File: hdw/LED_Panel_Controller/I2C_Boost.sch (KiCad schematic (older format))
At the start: 7 parts

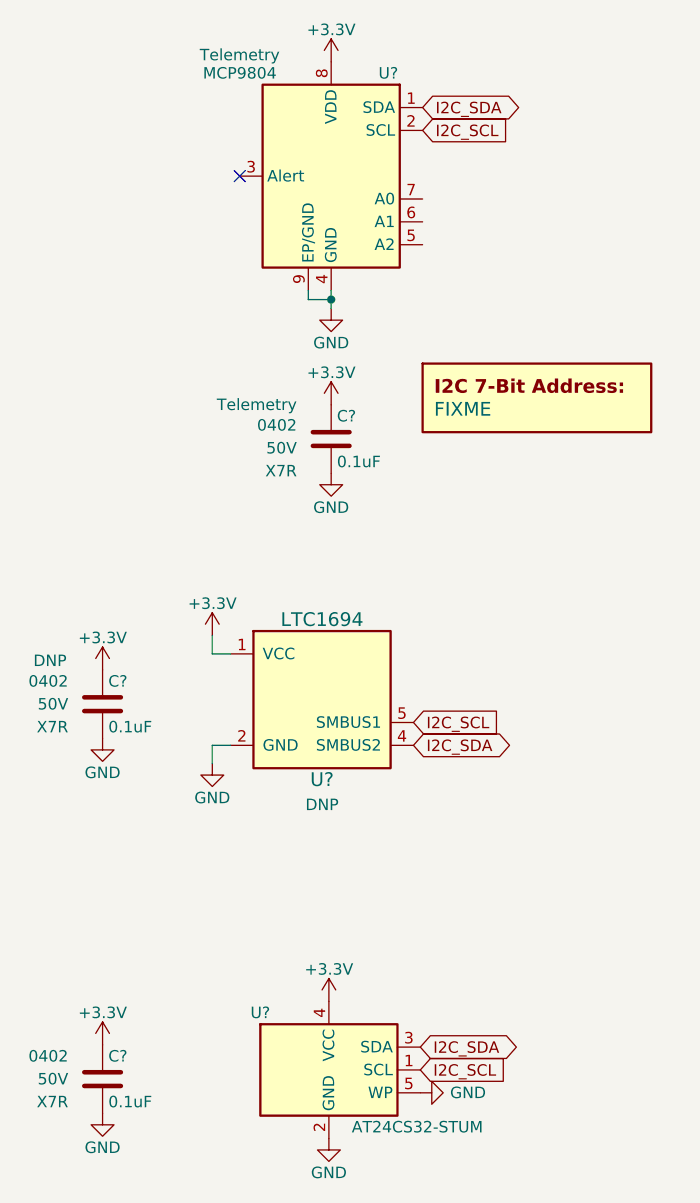
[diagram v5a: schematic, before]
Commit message: assigned I2C addresses
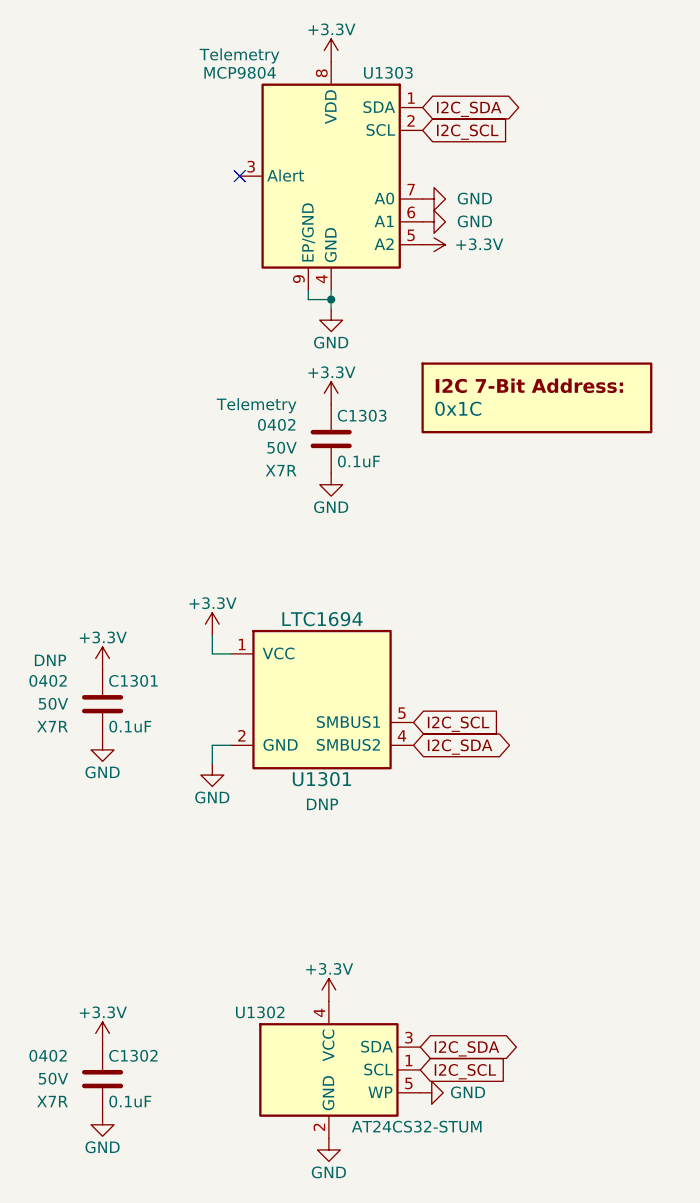
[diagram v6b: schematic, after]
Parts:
- DOC1301: renamed from DOC?; value FIXME -> 0x1C
- gave numbers to parts that had none: 6
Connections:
- net +3V3: now also U1303.5 (A2)
- net GND: now also U1303.6 (A1), U1303.7 (A0)
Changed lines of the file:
@@
 $EndDescr
 $Comp
-L Custom_Library:LTC1694 U?
+L Custom_Library:LTC1694 U1301
 U 1 1 5F6A42D0
 P 5300 3760
-F 0 "U?" H 5300 3410 60  0000 C CNN
+F 0 "U1301" H 5300 3410 60  0000 C CNN
 F 1 "LTC1694" H 5300 4110 60  0000 C CNN
 F 2 "Package_TO_SOT_SMD:SOT-23-5" H 5200 4060 60  0001 C CNN
@@
 $EndComp
 $Comp
-L power:+3.3V #PWR?
+L power:+3.3V #PWR01305
 U 1 1 5F6A5589
 P 4820 3480
-F 0 "#PWR?" H 4820 3330 50  0001 C CNN
+F 0 "#PWR01305" H 4820 3330 50  0001 C CNN
 F 1 "+3.3V" H 4820 3620 50  0000 C CNN
 F 2 "" H 4820 3480 50  0001 C CNN
@@
 	4820 3560 4900 3560
 $Comp
-L power:GND #PWR?
+L power:GND #PWR01306
 U 1 1 5F6A5AAB
 P 4820 4040
-F 0 "#PWR?" H 4820 3790 50  0001 C CNN
+F 0 "#PWR01306" H 4820 3790 50  0001 C CNN
 F 1 "GND" H 4820 3890 50  0000 C CNN
 F 2 "" H 4820 4040 50  0001 C CNN
@@
 	4820 3960 4900 3960
 $Comp
-L power:GND #PWR?
+L power:GND #PWR01302
 U 1 1 5F6A9D7C
 P 4340 3930
-F 0 "#PWR?" H 4340 3680 50  0001 C CNN
+F 0 "#PWR01302" H 4340 3680 50  0001 C CNN
 F 1 "GND" H 4340 3780 50  0000 C CNN
 F 2 "" H 4340 3930 50  0001 C CNN
@@
 AR Path="/5EAE3021/5F6A9DE1" Ref="C?"  Part="1"
 AR Path="/5F582A92/5F6A9DE1" Ref="C?"  Part="1"
-AR Path="/5F582A7C/5F6A9DE1" Ref="C?"  Part="1"
-F 0 "C?" H 4365 3880 50  0000 L CNN
+AR Path="/5F582A7C/5F6A9DE1" Ref="C1301"  Part="1"
+F 0 "C1301" H 4365 3880 50  0000 L CNN
 F 1 "0.1uF" H 4365 3680 50  0000 L CNN
 F 2 "Capacitors_SMD:C_0402" H 4378 3630 50  0001 C CNN
@@
 $EndComp
 $Comp
-L power:+3.3V #PWR?
+L power:+3.3V #PWR01301
 U 1 1 5F6AB1EB
 P 4340 3630
-F 0 "#PWR?" H 4340 3480 50  0001 C CNN
+F 0 "#PWR01301" H 4340 3480 50  0001 C CNN
 F 1 "+3.3V" H 4340 3770 50  0000 C CNN
 F 2 "" H 4340 3630 50  0001 C CNN
@@
 P 5330 5380
 AR Path="/5F5829EF/601A8ABF" Ref="U?"  Part="1"
-AR Path="/5F582A7C/601A8ABF" Ref="U?"  Part="1"
-F 0 "U?" H 5030 5630 50  0000 C CNN
+AR Path="/5F582A7C/601A8ABF" Ref="U1302"  Part="1"
+F 0 "U1302" H 5030 5630 50  0000 C CNN
 F 1 "AT24CS32-STUM" H 5430 5130 50  0000 L CNN
 F 2 "Package_TO_SOT_SMD:SOT-23-5" H 5330 5380 50  0001 C CNN
@@
 P 5330 5680
 AR Path="/5F5829EF/601A8AC5" Ref="#PWR?"  Part="1"
-AR Path="/5F582A7C/601A8AC5" Ref="#PWR?"  Part="1"
-F 0 "#PWR?" H 5330 5430 50  0001 C CNN
+AR Path="/5F582A7C/601A8AC5" Ref="#PWR01308"  Part="1"
+F 0 "#PWR01308" H 5330 5430 50  0001 C CNN
 F 1 "GND" H 5330 5530 50  0000 C CNN
 F 2 "" H 5330 5680 50  0001 C CNN
@@
 P 5330 5080
 AR Path="/5F5829EF/601A8ACB" Ref="#PWR?"  Part="1"
-AR Path="/5F582A7C/601A8ACB" Ref="#PWR?"  Part="1"
-F 0 "#PWR?" H 5330 4930 50  0001 C CNN
+AR Path="/5F582A7C/601A8ACB" Ref="#PWR01307"  Part="1"
+F 0 "#PWR01307" H 5330 4930 50  0001 C CNN
 F 1 "+3.3V" H 5330 5220 50  0000 C CNN
 F 2 "" H 5330 5080 50  0001 C CNN
@@
 $EndComp
 $Comp
-L power:GND #PWR?
+L power:GND #PWR01304
 U 1 1 601A97E7
 P 4340 5570
-F 0 "#PWR?" H 4340 5320 50  0001 C CNN
+F 0 "#PWR01304" H 4340 5320 50  0001 C CNN
 F 1 "GND" H 4340 5420 50  0000 C CNN
 F 2 "" H 4340 5570 50  0001 C CNN
@@
 AR Path="/5EAE3021/601A97F2" Ref="C?"  Part="1"
 AR Path="/5F582A92/601A97F2" Ref="C?"  Part="1"
-AR Path="/5F582A7C/601A97F2" Ref="C?"  Part="1"
-F 0 "C?" H 4365 5520 50  0000 L CNN
+AR Path="/5F582A7C/601A97F2" Ref="C1302"  Part="1"
+F 0 "C1302" H 4365 5520 50  0000 L CNN
 F 1 "0.1uF" H 4365 5320 50  0000 L CNN
 F 2 "Capacitors_SMD:C_0402" H 4378 5270 50  0001 C CNN
@@
 $EndComp
 $Comp
-L power:+3.3V #PWR?
+L power:+3.3V #PWR01303
 U 1 1 601A97F8
 P 4340 5270
-F 0 "#PWR?" H 4340 5120 50  0001 C CNN
+F 0 "#PWR01303" H 4340 5120 50  0001 C CNN
 F 1 "+3.3V" H 4340 5410 50  0000 C CNN
 F 2 "" H 4340 5270 50  0001 C CNN
@@
 P 5730 5480
 AR Path="/5F5829EF/601AB410" Ref="#PWR?"  Part="1"
-AR Path="/5F582A7C/601AB410" Ref="#PWR?"  Part="1"
-F 0 "#PWR?" H 5730 5230 50  0001 C CNN
+AR Path="/5F582A7C/601AB410" Ref="#PWR01313"  Part="1"
+F 0 "#PWR01313" H 5730 5230 50  0001 C CNN
 F 1 "GND" V 5730 5350 50  0000 R CNN
 F 2 "" H 5730 5480 50  0001 C CNN
@@
 AR Path="/5F581B77/6061CC13" Ref="#PWR?"  Part="1"
 AR Path="/5F581BB7/6061CC13" Ref="#PWR?"  Part="1"
-AR Path="/5F582A7C/6061CC13" Ref="#PWR?"  Part="1"
-F 0 "#PWR?" H 5340 1800 50  0001 C CNN
+AR Path="/5F582A7C/6061CC13" Ref="#PWR01310"  Part="1"
+F 0 "#PWR01310" H 5340 1800 50  0001 C CNN
 F 1 "GND" H 5340 1900 50  0000 C CNN
 F 2 "" H 5340 2050 50  0001 C CNN
@@
 AR Path="/5F581B77/6061CC1E" Ref="#PWR?"  Part="1"
 AR Path="/5F581BB7/6061CC1E" Ref="#PWR?"  Part="1"
-AR Path="/5F582A7C/6061CC1E" Ref="#PWR?"  Part="1"
-F 0 "#PWR?" H 5340 820 50  0001 C CNN
+AR Path="/5F582A7C/6061CC1E" Ref="#PWR01309"  Part="1"
+F 0 "#PWR01309" H 5340 820 50  0001 C CNN
 F 1 "+3.3V" H 5340 1110 50  0000 C CNN
 F 2 "" H 5340 970 50  0001 C CNN
@@
 AR Path="/5F581B77/6061CC26" Ref="U?"  Part="1"
 AR Path="/5F581BB7/6061CC26" Ref="U?"  Part="1"
-AR Path="/5F582A7C/6061CC26" Ref="U?"  Part="1"
-F 0 "U?" H 5090 1920 50  0000 C CNN
+AR Path="/5F582A7C/6061CC26" Ref="U1303"  Part="1"
+F 0 "U1303" H 5090 1920 50  0000 C CNN
 F 1 "MCP9804" H 5740 1920 50  0000 C CNN
 F 2 "Package_DFN_QFN:DFN-8-1EP_3x2mm_P0.5mm_EP1.3x1.5mm" H 4240 970 50  0001 C CNN
@@
 AR Path="/5F581B77/6061CC2F" Ref="#PWR?"  Part="1"
 AR Path="/5F581BB7/6061CC2F" Ref="#PWR?"  Part="1"
-AR Path="/5F582A7C/6061CC2F" Ref="#PWR?"  Part="1"
-F 0 "#PWR?" H 5340 2320 50  0001 C CNN
+AR Path="/5F582A7C/6061CC2F" Ref="#PWR01311"  Part="1"
+F 0 "#PWR01311" H 5340 2320 50  0001 C CNN
 F 1 "+3.3V" H 5340 2610 50  0000 C CNN
 F 2 "" H 5340 2470 50  0001 C CNN
@@
 AR Path="/5F581B77/6061CC35" Ref="#PWR?"  Part="1"
 AR Path="/5F581BB7/6061CC35" Ref="#PWR?"  Part="1"
-AR Path="/5F582A7C/6061CC35" Ref="#PWR?"  Part="1"
-F 0 "#PWR?" H 5340 2520 50  0001 C CNN
+AR Path="/5F582A7C/6061CC35" Ref="#PWR01312"  Part="1"
+F 0 "#PWR01312" H 5340 2520 50  0001 C CNN
 F 1 "GND" H 5340 2620 50  0000 C CNN
 F 2 "" H 5340 2770 50  0001 C CNN
@@
 AR Path="/5F581B77/6061CC3B" Ref="DOC?"  Part="1"
 AR Path="/5F581BB7/6061CC3B" Ref="DOC?"  Part="1"
-AR Path="/5F582A7C/6061CC3B" Ref="DOC?"  Part="1"
-F 0 "DOC?" H 6240 2740 60  0001 C CNN
-F 1 "FIXME" H 5790 2490 60  0000 L CNN
+AR Path="/5F582A7C/6061CC3B" Ref="DOC1301"  Part="1"
+F 0 "DOC1301" H 6240 2740 60  0001 C CNN
+F 1 "0x1C" H 5790 2490 60  0000 L CNN
 F 2 "" H 6240 2840 60  0001 C CNN
 F 3 "" H 6240 2840 60  0001 C CNN
@@
 AR Path="/5F581B77/6061CC45" Ref="C?"  Part="1"
 AR Path="/5F581BB7/6061CC45" Ref="C?"  Part="1"
-AR Path="/5F582A7C/6061CC45" Ref="C?"  Part="1"
-F 0 "C?" H 5365 2720 50  0000 L CNN
+AR Path="/5F582A7C/6061CC45" Ref="C1303"  Part="1"
+F 0 "C1303" H 5365 2720 50  0000 L CNN
 F 1 "0.1uF" H 5365 2520 50  0000 L CNN
 F 2 "Capacitors_SMD:C_0402" H 5378 2470 50  0001 C CNN
@@
 	1    0    0    -1
 $EndComp
+$Comp
+L power:GND #PWR?
+U 1 1 6076C67B
+P 5740 1570
+AR Path="/5B3E071A/6076C67B" Ref="#PWR?"  Part="1"
+AR Path="/5E0652BA/6076C67B" Ref="#PWR?"  Part="1"
+AR Path="/5E0A0E29/6076C67B" Ref="#PWR?"  Part="1"
+AR Path="/5E052856/6076C67B" Ref="#PWR?"  Part="1"
+AR Path="/5EAE2D84/6076C67B" Ref="#PWR?"  Part="1"
+AR Path="/5F581B58/6076C67B" Ref="#PWR?"  Part="1"
+AR Path="/5F581B77/6076C67B" Ref="#PWR?"  Part="1"
+AR Path="/5F5829EF/6076C67B" Ref="#PWR?"  Part="1"
+AR Path="/5F582A7C/6076C67B" Ref="#PWR01314"  Part="1"
+F 0 "#PWR01314" H 5740 1320 50  0001 C CNN
+F 1 "GND" V 5740 1420 50  0000 R CNN
+F 2 "" H 5740 1570 50  0001 C CNN
+F 3 "" H 5740 1570 50  0001 C CNN
+	1    5740 1570
+	0    -1   1    0
+$EndComp
+$Comp
+L power:+3.3V #PWR?
+U 1 1 6076C681
+P 5740 1770
+AR Path="/5E0652BA/6076C681" Ref="#PWR?"  Part="1"
+AR Path="/5E0A0E29/6076C681" Ref="#PWR?"  Part="1"
+AR Path="/5E052856/6076C681" Ref="#PWR?"  Part="1"
+AR Path="/5EAE2D84/6076C681" Ref="#PWR?"  Part="1"
+AR Path="/5F581B58/6076C681" Ref="#PWR?"  Part="1"
+AR Path="/5F581B77/6076C681" Ref="#PWR?"  Part="1"
+AR Path="/5F5829EF/6076C681" Ref="#PWR?"  Part="1"
+AR Path="/5F582A7C/6076C681" Ref="#PWR01316"  Part="1"
+F 0 "#PWR01316" H 5740 1620 50  0001 C CNN
+F 1 "+3.3V" V 5740 1910 50  0000 L CNN
+F 2 "" H 5740 1770 50  0001 C CNN
+F 3 "" H 5740 1770 50  0001 C CNN
+	1    5740 1770
+	0    1    -1   0
+$EndComp
+$Comp
+L power:GND #PWR?
+U 1 1 6076C8FF
+P 5740 1670
+AR Path="/5B3E071A/6076C8FF" Ref="#PWR?"  Part="1"
+AR Path="/5E0652BA/6076C8FF" Ref="#PWR?"  Part="1"
+AR Path="/5E0A0E29/6076C8FF" Ref="#PWR?"  Part="1"
+AR Path="/5E052856/6076C8FF" Ref="#PWR?"  Part="1"
+AR Path="/5EAE2D84/6076C8FF" Ref="#PWR?"  Part="1"
+AR Path="/5F581B58/6076C8FF" Ref="#PWR?"  Part="1"
+AR Path="/5F581B77/6076C8FF" Ref="#PWR?"  Part="1"
+AR Path="/5F5829EF/6076C8FF" Ref="#PWR?"  Part="1"
+AR Path="/5F582A7C/6076C8FF" Ref="#PWR01315"  Part="1"
+F 0 "#PWR01315" H 5740 1420 50  0001 C CNN
+F 1 "GND" V 5740 1520 50  0000 R CNN
+F 2 "" H 5740 1670 50  0001 C CNN
+F 3 "" H 5740 1670 50  0001 C CNN
+	1    5740 1670
+	0    -1   1    0
+$EndComp
 $EndSCHEMATC
